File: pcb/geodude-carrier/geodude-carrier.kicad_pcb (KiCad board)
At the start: 2 copper layers, 140 x 149 mm, 43 parts, among them J1 12V, J2 12V, J3 GND, J31 SCL, J32 SDA, J34 3V3, J37 5V, J39 GND_L, J4 GND, J40 SCL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

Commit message: Added back silkscreen quote, Gerbers updated
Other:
- board text added: ""uhm I don't fuckin know.\nalright that's going on it\nyou didn't put that?\nyou didn't put that right\nall those things that we said are going on it\nyou're not typing what I'm saying right? no you're not stop typing"\n- Zeul and Mizi March 30th 2026"
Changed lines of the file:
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@@
 		(layer "Edge.Cuts")
+	)
+	(gr_text "\"uhm I don't fuckin know.\\nalright that's going on it\\nyou didn't put that?\\nyou didn't put that right\\nall those things that we said are going on it\\nyou're not typing what I'm saying right? no you're not stop typing\"\\n- Zeul and Mizi March 30th 2026"
+		(at 75 80 0)
+		(layer "B.SilkS")
+		(effects
+			(font
+				(size 1.2 1.2)
+				(thickness 0.15)
+			)
+			(justify mirror)
+		)
 	)
 	(segment

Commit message: Edge adjustment
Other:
- board text added: "uhm I don't fuckin know. alright that's going on it you didn't put that? you didn't put that right all those things that we said are going on it you're not typing what I'm saying right? no you're not stop typing - Zeul and Mizi March 30th 2026"
- board text removed: ""uhm I don't fuckin know.\nalright that's going on it\nyou didn't put that?\nyou didn't put that right\nall those things that we said are going on it\nyou're not typing what I'm saying right? no you're not stop typing"\n- Zeul and Mizi March 30th 2026"
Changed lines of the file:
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@@
 		(layer "Edge.Cuts")
 	)
-	(gr_text "\"uhm I don't fuckin know.\\nalright that's going on it\\nyou didn't put that?\\nyou didn't put that right\\nall those things that we said are going on it\\nyou're not typing what I'm saying right? no you're not stop typing\"\\n- Zeul and Mizi March 30th 2026"
-		(at 75 80 0)
+	(gr_text "uhm I don't fuckin know.\nalright that's going on it\nyou didn't put that?\nyou didn't put that right\nall those things that we said are going on it\nyou're not typing what I'm saying right? no you're not stop typing\n- Zeul and Mizi March 30th 2026"
+		(at 69.1 27.6 0)
 		(layer "B.SilkS")
 		(effects
@@
 				(thickness 0.15)
 			)
-			(justify mirror)
+			(justify left mirror)
 		)
 	)

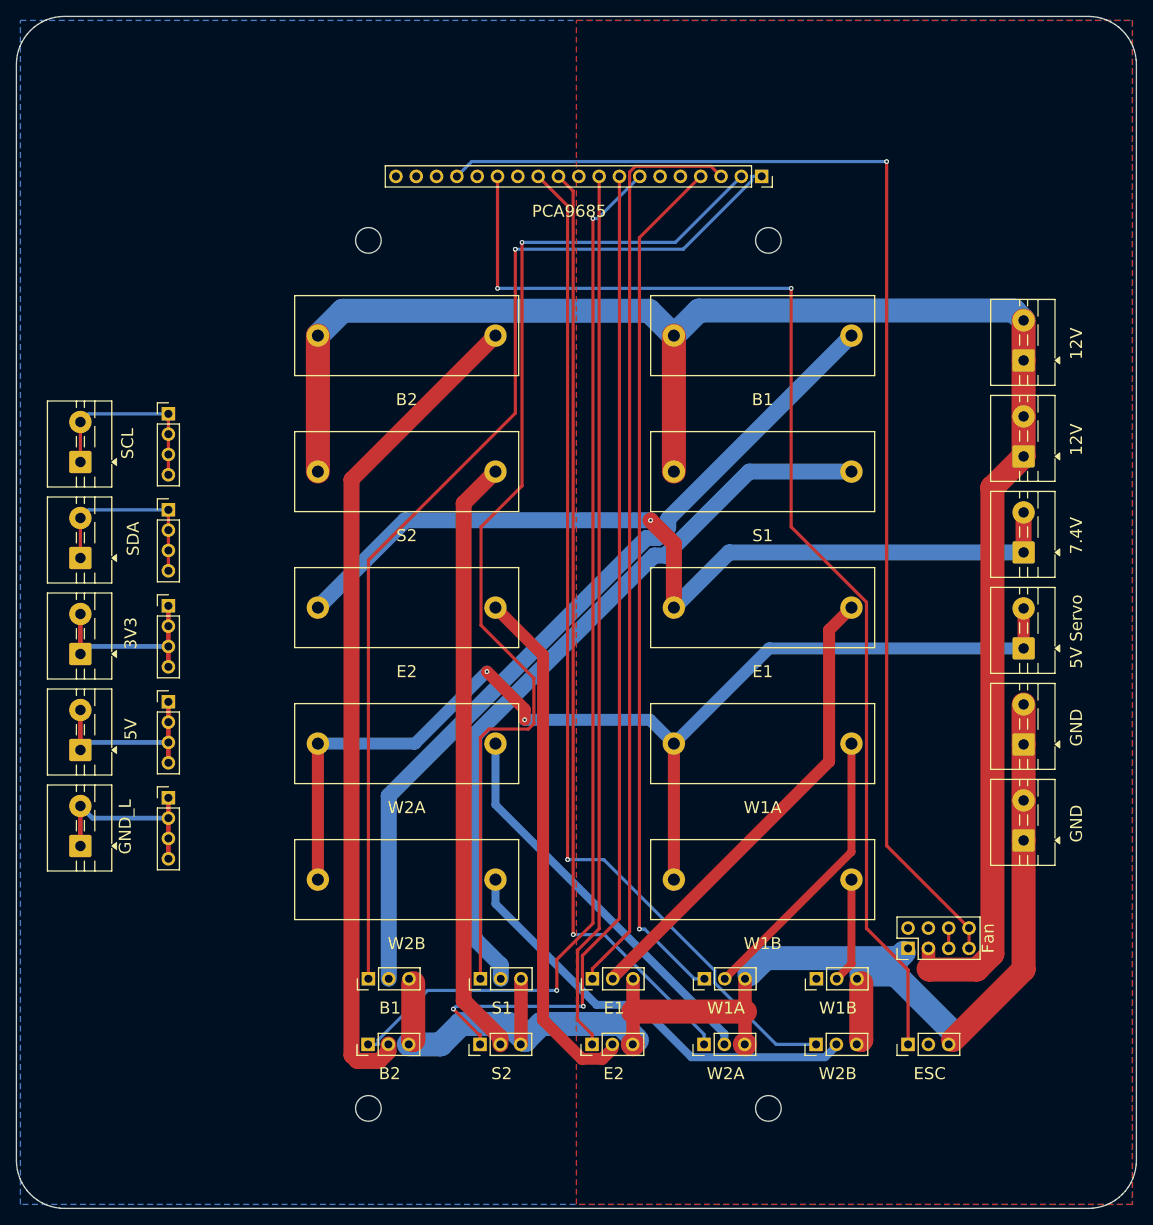
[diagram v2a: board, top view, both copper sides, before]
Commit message: Tighter board 140x136mm 6mm corners, 289 tracks, 0 unconnected, 0 electrical violations
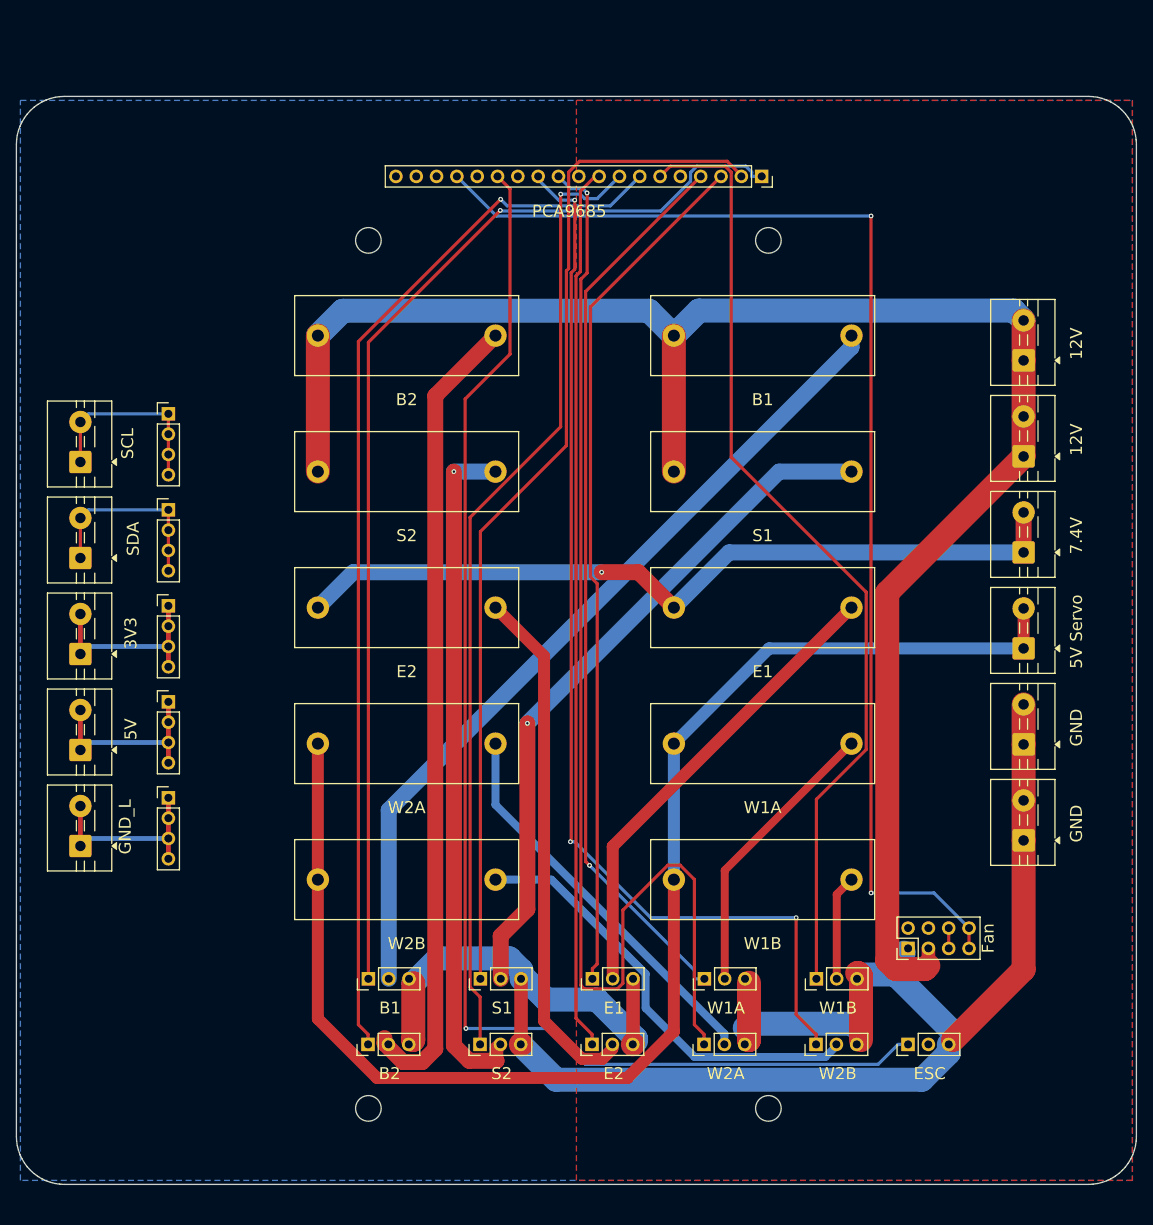
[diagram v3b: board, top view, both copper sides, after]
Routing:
- net PWM_CH4: track 0.00 -> 120.1 mm
- net GND: track 176.5 -> 222.7 mm
- net +5V_SERVO: track 140.4 -> 174.0 mm, vias 2 -> 0
- net PWM_CH8: track 118.3 -> 151.8 mm
- net PWM_CH11: track 151.3 -> 167.7 mm, vias 2 -> 1
- net SV7_PWR: track 75.1 -> 85.3 mm, vias 0 -> 1
- net +7V4: track 109.8 -> 99.7 mm
- net PWM_CH6: track 128.0 -> 120.2 mm, vias 2 -> 1
- net PWM_CH2: track 115.0 -> 107.7 mm
- net PWM_CH9: track 128.5 -> 135.5 mm, vias 1 -> 3
- net SV2_PWR: track 92.6 -> 86.9 mm, vias 0 -> 1
- net PWM_CH0: track 133.7 -> 139.4 mm
- net PWM_CH3: track 108.0 -> 113.1 mm
- net PWM_CH1: track 133.4 -> 128.4 mm, vias 1 -> 0
- net +12V: track 218.8 -> 221.6 mm
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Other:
- board size 140 x 149 mm -> 140 x 136 mm

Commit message: Board 140x134mm, fan +12V thin trace, render, 1 unconnected PWM, Gerbers ready
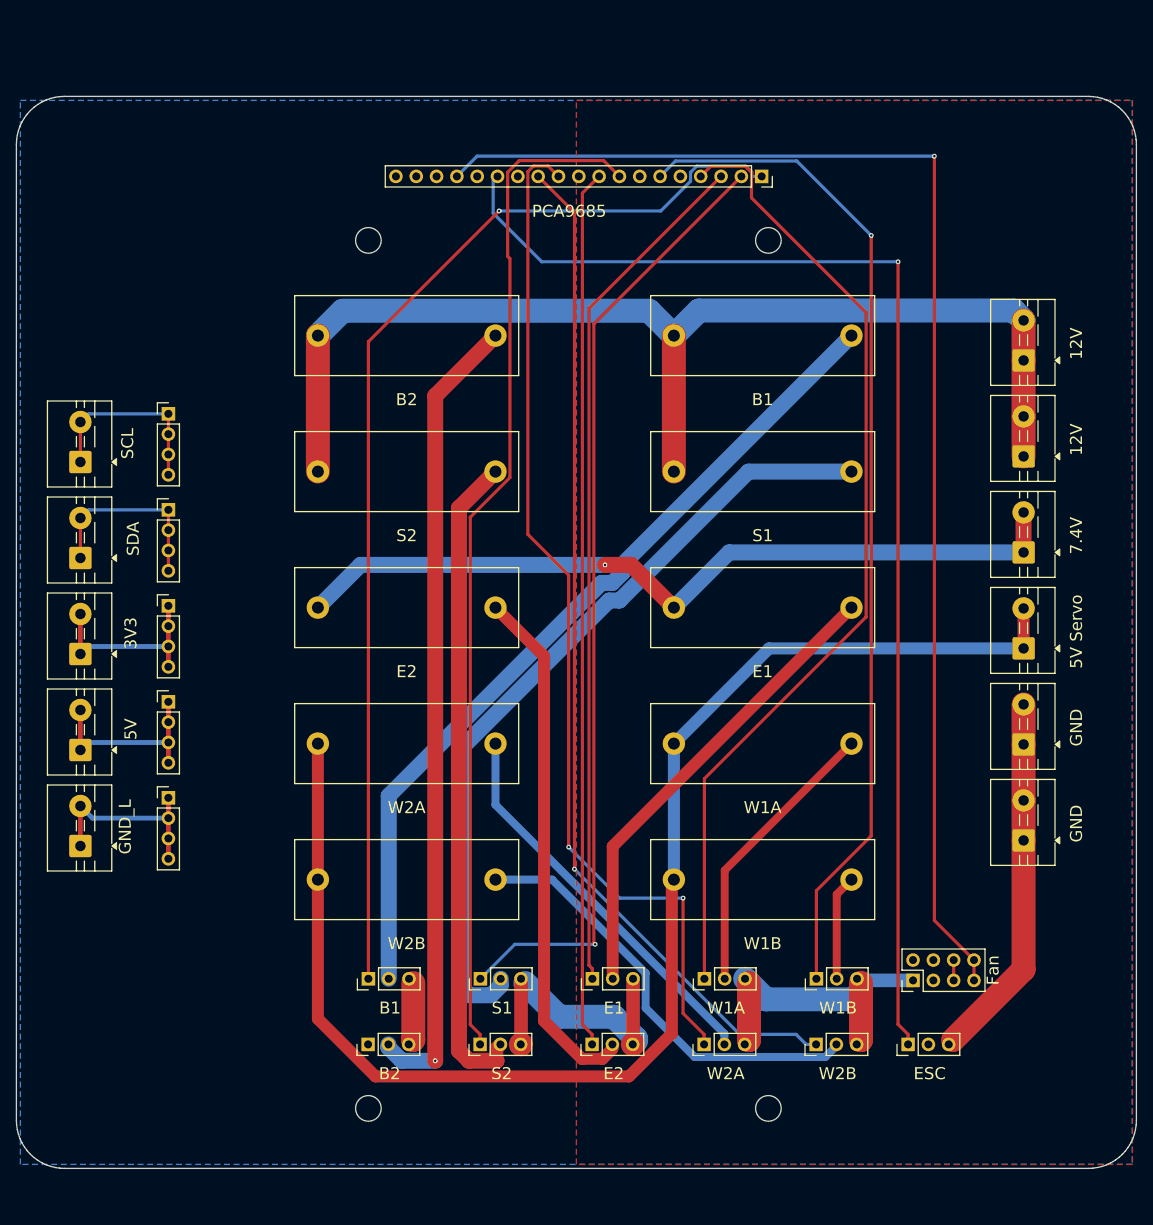
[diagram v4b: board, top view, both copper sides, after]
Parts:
- moved J_FAN 4.05 mm to (117.1, 124.5)
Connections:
- J_FAN pad 3: +12V -> +12V_FAN
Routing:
- net PWM_CH5: track 132.8 -> 0.00 mm, vias 1 -> 0
- net GND: track 222.7 -> 131.5 mm
- net +12V: track 221.6 -> 143.6 mm
- net PWM_CH8: track 151.8 -> 127.5 mm, vias 1 -> 2
- net SV2_PWR: track 86.9 -> 99.4 mm, vias 1 -> 0
- net PWM_CH11: track 167.7 -> 156.3 mm
- net PWM_CH12: track 155.0 -> 165.8 mm, vias 2 -> 1
- net PWM_CH3: track 113.1 -> 122.3 mm, vias 1 -> 0
- net PWM_CH1: track 128.4 -> 119.8 mm, vias 0 -> 1
- net PWM_CH9: track 135.5 -> 127.7 mm, vias 3 -> 1
- net PWM_CH6: track 120.2 -> 127.1 mm, vias 1 -> 0
- net PWM_CH4: track 120.1 -> 126.8 mm, vias 0 -> 1
- net SV7_PWR: track 85.3 -> 81.8 mm, vias 1 -> 0
- net SV6_PWR: track 101.9 -> 100.7 mm, vias 0 -> 1
- net PWM_CH7: track 110.8 -> 109.9 mm
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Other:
- board size 140 x 136 mm -> 140 x 134 mm

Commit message: Single servo row, ESC/Fan above, 140x134mm, render, Gerbers
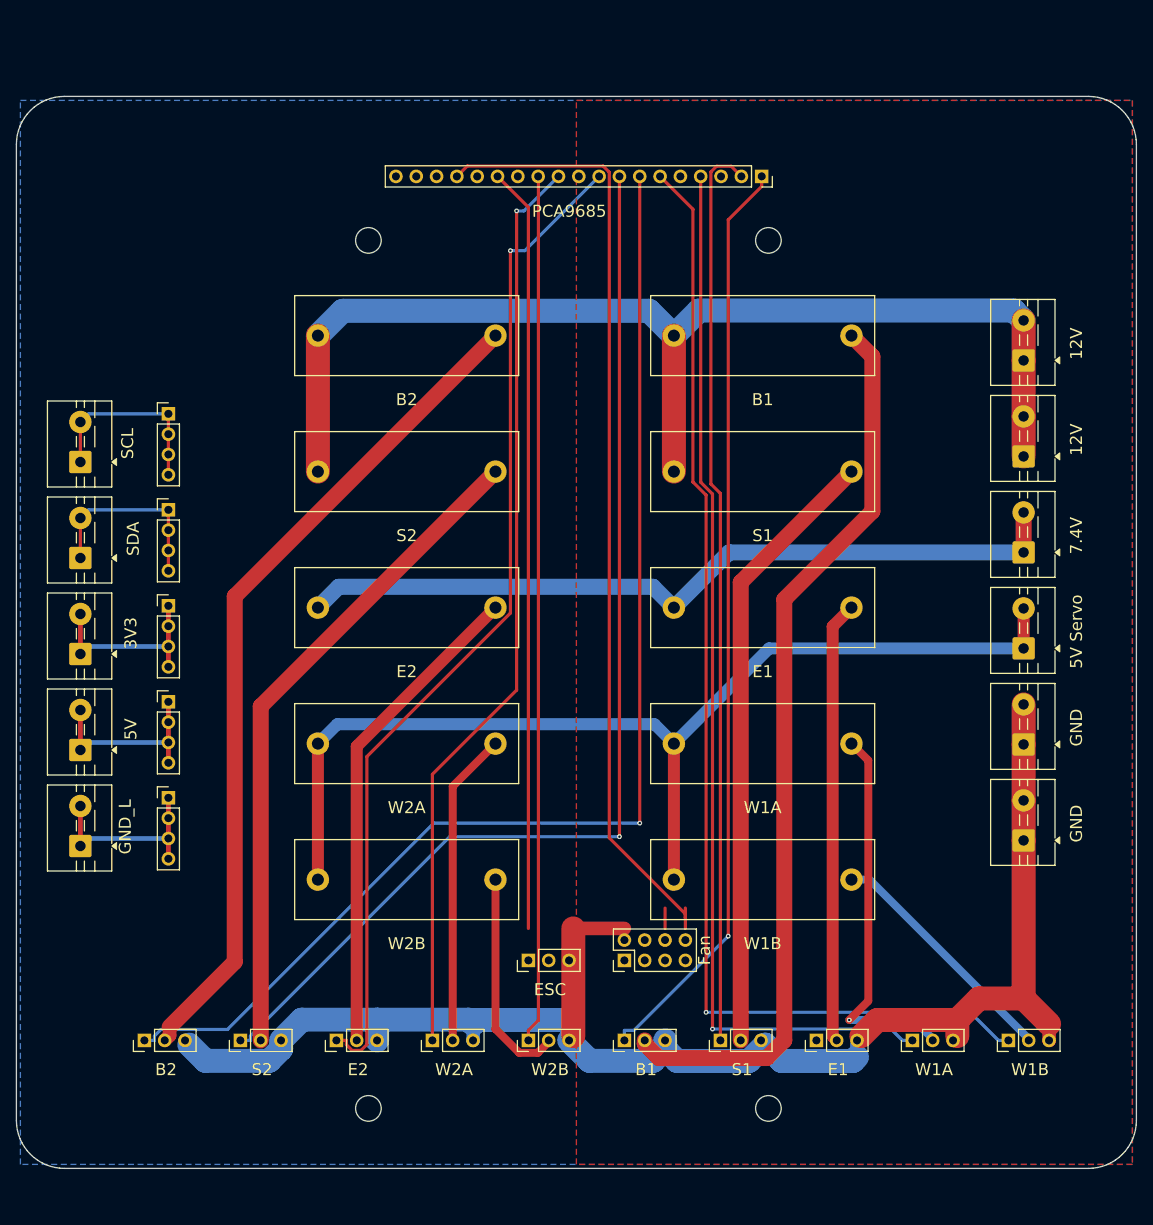
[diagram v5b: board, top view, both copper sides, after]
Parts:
- moved J_ESC 48.6 mm to (69.0, 122.0)
- moved J_FAN 36.2 mm to (81.0, 122.0)
- moved SV10 36.0 mm to (69.0, 132.0)
- moved SV9 34.0 mm to (57.0, 132.0)
- moved SV1 32.9 mm to (81.0, 132.0)
- moved SV8 32.0 mm to (45.0, 132.0)
- moved SV2 31.0 mm to (93.0, 132.0)
- moved SV7 30.0 mm to (33.0, 132.0)
- moved SV3 29.0 mm to (105.0, 132.0)
- moved SV6 28.0 mm to (21.0, 132.0)
- moved SV4 27.1 mm to (117.0, 132.0)
- moved SV5 25.2 mm to (129.0, 132.0)
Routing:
- net PWM_CH5: track 0.00 -> 154.3 mm, vias 0 -> 1
- net PWM_CH2: track 107.3 -> 0.00 mm
- net GND: track 131.5 -> 193.5 mm
- net PWM_CH11: track 156.3 -> 95.6 mm, vias 1 -> 0
- net PWM_CH12: track 165.8 -> 119.6 mm, vias 1 -> 0
- net +5V_SERVO: track 173.8 -> 134.1 mm
- net SV10_PWR: track 55.1 -> 27.3 mm
- net PWM_CH0: track 139.4 -> 115.8 mm
- net SV2_PWR: track 99.4 -> 76.8 mm
- net PWM_CH4: track 126.8 -> 146.1 mm
- net PWM_CH9: track 127.7 -> 108.5 mm, vias 1 -> 0
- net SV5_PWR: track 13.2 -> 30.6 mm
- net PWM_CH7: track 109.9 -> 126.6 mm, vias 0 -> 1
- net PWM_CH6: track 127.1 -> 140.8 mm, vias 0 -> 1
- net PWM_CH8: track 127.5 -> 115.1 mm, vias 2 -> 1
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
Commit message: Placement update
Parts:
- moved J_FAN 51.1 mm to (127.4, 143.3)
- moved J_ESC 48.6 mm to (113.4, 141.6)
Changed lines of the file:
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@@
 	(footprint "PinHeader_2x04_P2.54mm_Vertical"
 		(layer "F.Cu")
-		(at 81 122 90)
+		(at 127.42 143.34 90)
 		(descr "Through hole straight pin header, 2x04, 2.54mm pitch, double rows")
 		(tags "Through hole pin header THT 2x04 2.54mm double row")
@@
 		)
 		(fp_text user "${REFERENCE}"
-			(at 1.27 3.81 180)
+			(at 1.2 3.92 180)
 			(layer "F.Fab")
 			(effects
@@
 	(footprint "PinHeader_1x03_P2.54mm_Vertical"
 		(layer "F.Cu")
-		(at 69 122 90)
+		(at 113.42 141.6 90)
 		(descr "Through hole straight pin header, 1x03, 2.54mm pitch, single row")
 		(tags "Through hole pin header THT 1x03 2.54mm single row")
